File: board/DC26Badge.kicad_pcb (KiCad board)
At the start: 2 copper layers, 94 x 46.5 mm, 23 parts, among them J1 PWR_HDR, J2 PWR_CONN, J3 VOLTMETER, J4 AMMETER, J5 Cortex_SWD, SW1 JOYSTICK, SW2 SW_Push, U1 HT16K33-28, U2 BT832

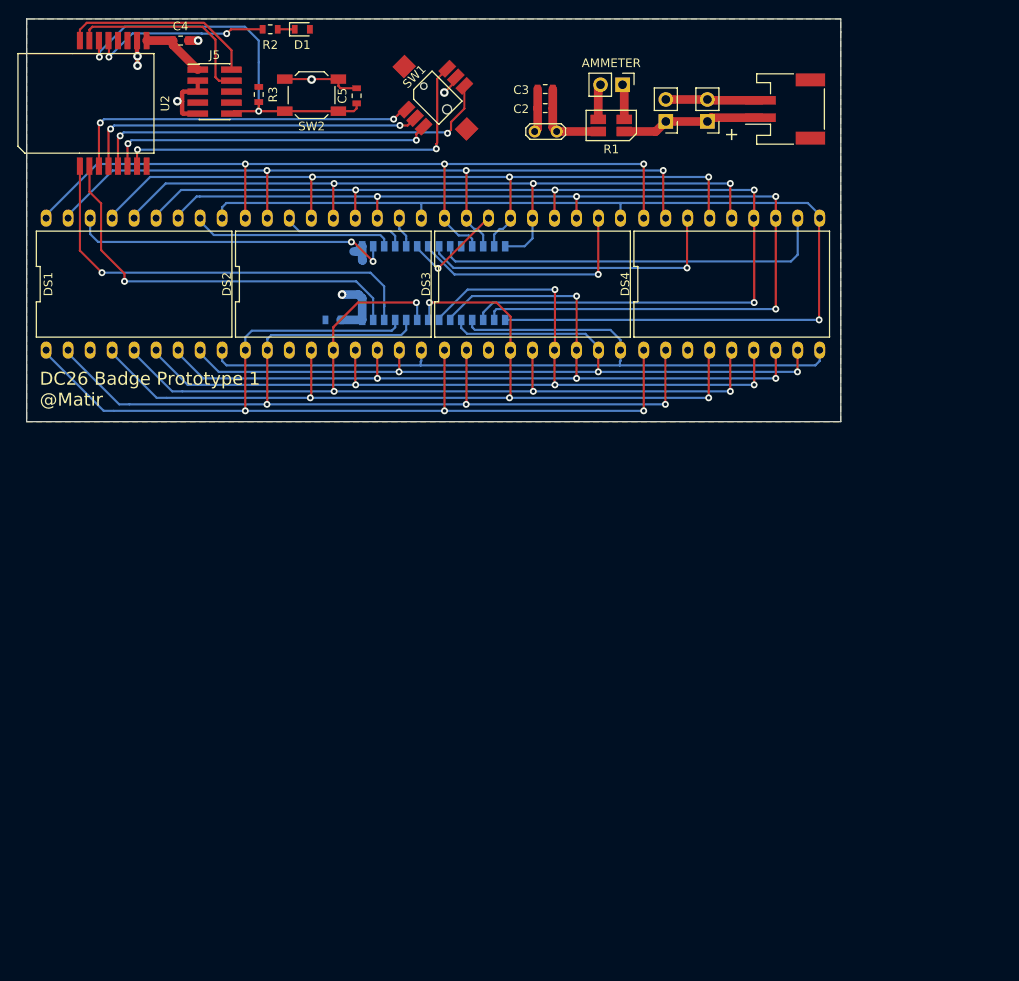
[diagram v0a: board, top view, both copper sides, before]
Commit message: Do first circular board.
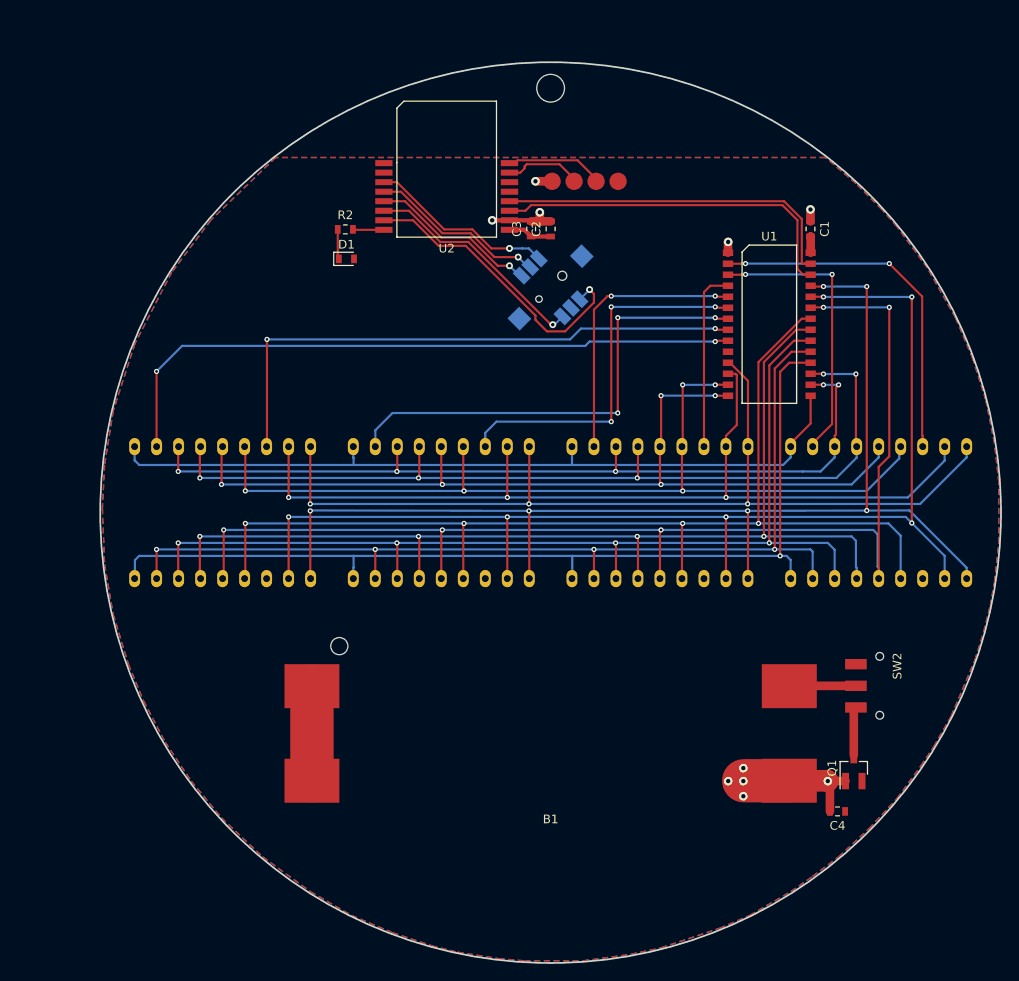
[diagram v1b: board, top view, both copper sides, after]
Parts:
- removed C5: 0.1u, Capacitor_SMD:C_0603_1608Metric
- removed J2: PWR_CONN, Connector_JST:JST_PH_S2B-PH-SM4-TB_1x02_P2.00mm_Horizontal
- removed J3: VOLTMETER, PinHeaders:Pin_Header_Straight_1x02_Pitch2.54mm
- removed J4: AMMETER, PinHeaders:Pin_Header_Straight_1x02_Pitch2.54mm
- removed J5: Cortex_SWD, Connector_PinHeader_1.27mm:PinHeader_2x05_P1.27mm_Vertical_SMD
- removed R1: 0.1, DC26badge:FC4T
- removed R3: 1k, Resistor_SMD:R_0603_1608Metric
- removed TP1: PWRTP, TestPoint:TestPoint_2Pads_Pitch2.54mm_Drill0.8mm
- added B1: Dual_AAA_Holder, DC26badge:Keystone_1022, F.Cu at (155.5, 106.0)
- added G***: LOGO, DC26badge:BG_GLOBE, B.Cu at (155.5, 80.0)
- added MK1: Mounting_Hole, MountingHole:MountingHole_3.2mm_M3, F.Cu at (155.5, 31.5)
- added Q1: SSM3J338, Package_TO_SOT_SMD:SOT-23_Handsoldering, F.Cu at (190.5, 110.0)
- C1: moved to F.Cu
- DS1, DS2, DS3, DS4, SW1: moved to B.Cu
- J1: value PWR_HDR -> SWD_POGO; footprint PinHeaders:Pin_Header_Straight_1x02_Pitch2.54mm -> DC26badge:SWD_POGO
- SW2: value SW_Push -> SW_SPDT; footprint Button_Switch_SMD:SW_SPST_SKQG -> DC26badge:JS102011SAQN
- U1: footprint DC26badge:SOIC-28-300mil -> DC26badge:HT16K133; moved to F.Cu
- moved C4 116.9 mm to (188.6, 115.0), turned to 180 degrees
- moved SW2 94.6 mm to (193.5, 100.5), turned to 90 degrees
- moved DS1 89.9 mm to (193.4, 80.5), turned to 180 degrees
- moved DS4 64.4 mm to (117.6, 80.5), turned to 180 degrees
- moved C1 56.1 mm to (185.5, 47.8), turned to 270 degrees
- moved DS2 46.0 mm to (168.1, 80.5), turned to 180 degrees
- moved U2 40.0 mm to (143.5, 44.0), turned to 270 degrees
- moved U1 39.0 mm to (180.8, 58.8), turned to 270 degrees
- moved DS3 28.4 mm to (142.9, 80.5), turned to 180 degrees
- moved D1 27.0 mm to (131.9, 51.2)
- moved SW1 25.6 mm to (155.5, 54.5), turned to 45 degrees
- moved R2 24.7 mm to (131.8, 47.8), turned to 0 degrees
- moved C3 16.2 mm to (153.2, 47.8), turned to 90 degrees
- moved J1 15.7 mm to (159.5, 42.2)
- moved C2 14.0 mm to (155.5, 47.8), turned to 90 degrees
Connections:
- J1 pad 1: /P_IN -> VDD
- J1 pad 2: GND -> /SWDIO
- SW2 pad 1: /RESET -> Net-(Q1-Pad3)
- SW2 pad 2: GND -> Net-(B1-Pad1)
- U2 pad 1: /SCL -> Net-(U2-Pad1)
- U2 pad 11: Net-(U2-Pad11) -> /SCL
- U2 pad 12: Net-(U2-Pad12) -> /SDA
- U2 pad 13: /LED1 -> Net-(U2-Pad13)
- U2 pad 2: /SDA -> Net-(U2-Pad2)
- U2 pad 3: /UP -> /LT
- U2 pad 5: /DN -> /UP
- U2 pad 6: /LT -> /RT
- U2 pad 7: /RT -> /DN
- U2 pad 8: Net-(U2-Pad8) -> /LED1
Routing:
- net /RESET: track 47.3 -> 0.00 mm, vias 2 -> 0
- net /N: track 100.9 -> 138.8 mm, vias 4 -> 5
- net /B: track 123.0 -> 90.3 mm, vias 1 -> 0
- net /DIG4: track 11.9 -> 43.4 mm, vias 1 -> 3
- net /DIG6: track 35.9 -> 66.2 mm, vias 1 -> 2
- net /DIG7: track 46.1 -> 76.1 mm, vias 0 -> 2
- net /L: track 109.7 -> 139.6 mm, vias 3 -> 6
- net /DIG3: track 3.58 -> 32.0 mm, vias 0 -> 2
- net /DIG5: track 27.6 -> 54.5 mm, vias 1 -> 3
- net /A: track 121.9 -> 96.9 mm, vias 4 -> 5
- net /M: track 104.0 -> 127.1 mm
- net /E: track 113.3 -> 135.7 mm, vias 3 -> 6
- net /UP: track 41.7 -> 19.5 mm, vias 2 -> 1
- net /G1: track 122.8 -> 103.1 mm, vias 4 -> 5
- net /RT: track 46.2 -> 26.6 mm, vias 2 -> 1
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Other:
- board size 94 x 46.5 mm -> 104 x 104 mm
- rule via_min_size: 0.4 -> 0.6
- board text removed: "+"
- board text removed: "DC26 Badge Prototype 1 @Matir"

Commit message: Add copyright.
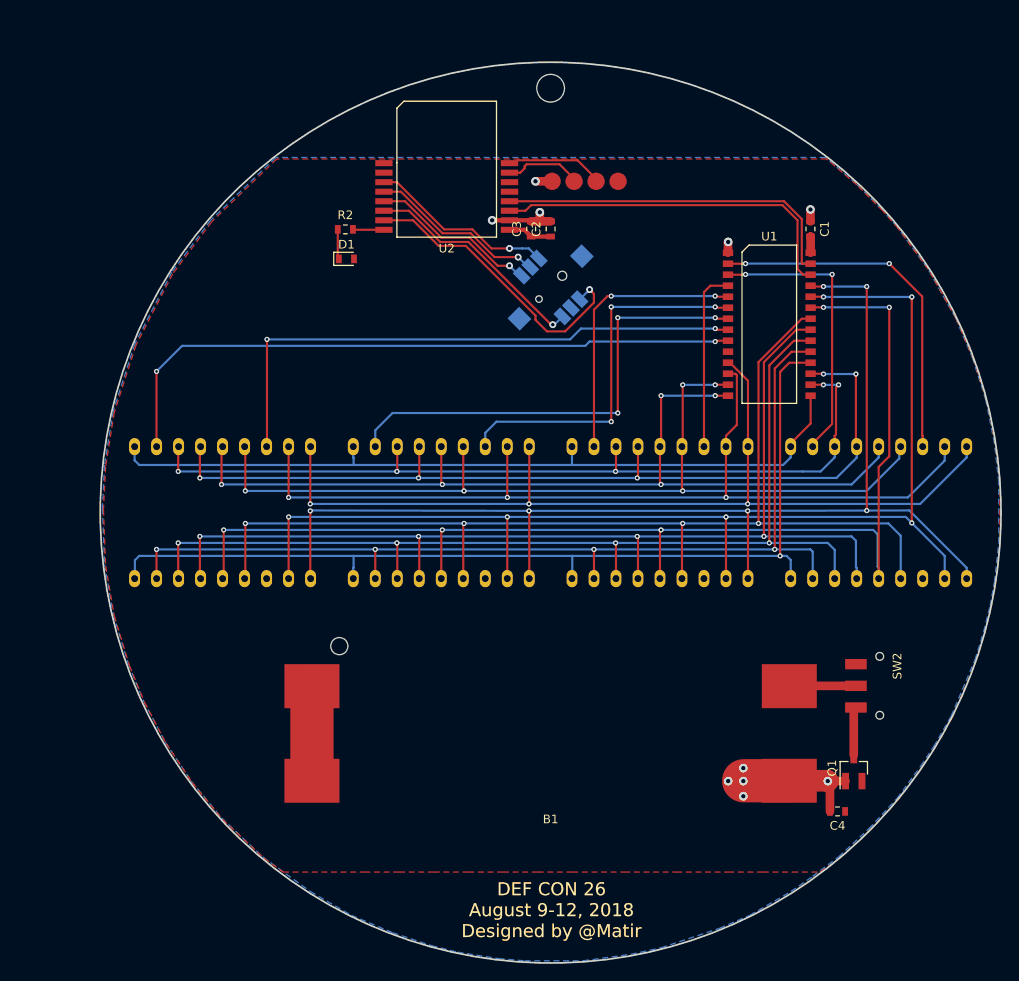
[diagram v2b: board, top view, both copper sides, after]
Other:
- board text added: "DEF CON 26 August 9-12, 2018 Designed by @Matir"
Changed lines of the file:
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@@
   (general
     (thickness 1.6)
-    (drawings 1)
+    (drawings 3)
     (tracks 499)
     (zones 0)
@@
       (xy 2.655607 -45.401114)) (layer B.SilkS) (width 0.01))
   )
+  (gr_text "DEF CON 26\nAugust 9-12, 2018\nDesigned by @Matir" (at 155.6 126.4) (layer F.SilkS)
+    (effects (font (size 1.5 1.5) (thickness 0.3)))
+  )
+  (gr_text "DEF CON 26\nAugust 9-12, 2018\nDesigned by @Matir" (at 155.6 126.4) (layer F.Cu)
+    (effects (font (size 1.5 1.5) (thickness 0.3)))
+  )
   (gr_circle (center 155.5 80.5) (end 207.5 80.5) (layer Edge.Cuts) (width 0.2))
   (segment (start 175.98 49.27) (end 176 49.25) (width 1) (layer F.Cu) (net 1))
@@
     )
   )
-  (zone (net 2) (net_name VDD) (layer F.Cu) (hatch edge 0.508)
-    (connect_pads (clearance 0.254))
-    (min_thickness 0.254)
-    (fill yes (arc_segments 16) (thermal_gap 0.254) (thermal_bridge_width 0.3))
-    (polygon
-      (pts
-        (xy 123.75 39.5) (xy 116.25 46.75) (xy 111.75 52.75) (xy 107.5 61) (xy 105 68.75)
-        (xy 104 75) (xy 103.75 80) (xy 104 86.5) (xy 105 92.25) (xy 106.75 98)
-        (xy 108.5 102.25) (xy 111 107) (xy 114 111.5) (xy 117.5 115.75) (xy 122.25 120.25)
-        (xy 127.75 124.25) (xy 132.5 127) (xy 137.25 129) (xy 141.75 130.5) (xy 144.75 131.25)
-        (xy 149.5 132) (xy 152.5 132.25) (xy 159.25 132.25) (xy 164.75 131.5) (xy 168.25 130.75)
-        (xy 175 128.5) (xy 178.5 127) (xy 183.25 124.25) (xy 185.75 122.5) (xy 188.75 120.25)
-        (xy 192.25 117) (xy 195.5 113.5) (xy 198.25 109.75) (xy 199.75 107.5) (xy 201.75 104)
-        (xy 204.5 97.5) (xy 205.5 94.25) (xy 206.25 91.25) (xy 206.75 88.5) (xy 207.25 84)
-        (xy 207.25 77) (xy 206.75 72.5) (xy 205.75 67.5) (xy 204.25 62.75) (xy 202.25 58)
-        (xy 199 52.25) (xy 195.5 47.5) (xy 193.75 45.5) (xy 190.75 42.5) (xy 187.25 39.5)
-      )
-    )
-  )
   (zone (net 1) (net_name GND) (layer B.Cu) (hatch edge 0.508)
     (connect_pads (clearance 0.254))
@@
       )
     )
+  )
+  (zone (net 2) (net_name VDD) (layer F.Cu) (hatch edge 0.508)
+    (connect_pads (clearance 0.254))
+    (min_thickness 0.254)
+    (fill yes (arc_segments 16) (thermal_gap 0.254) (thermal_bridge_width 0.3))
+    (polygon
+      (pts
+        (xy 123.870179 39.671493) (xy 116.370179 46.921493) (xy 111.870179 52.921493) (xy 107.620179 61.171493) (xy 105.120179 68.921493)
+        (xy 104.120179 75.171493) (xy 103.870179 80.171493) (xy 104.120179 86.671493) (xy 105.120179 92.421493) (xy 106.870179 98.171493)
+        (xy 108.620179 102.421493) (xy 111.120179 107.171493) (xy 114.120179 111.671493) (xy 117.620179 115.921493) (xy 122.4 120.4)
+        (xy 124.6 122) (xy 134 122) (xy 138 122) (xy 142 122) (xy 146 122)
+        (xy 150 122) (xy 154 122) (xy 158 122) (xy 164 122) (xy 170 122)
+        (xy 176 122) (xy 180 122) (xy 183.4 122) (xy 186.6 122) (xy 188.870179 120.421493)
+        (xy 192.370179 117.171493) (xy 195.620179 113.671493) (xy 198.370179 109.921493) (xy 199.870179 107.671493) (xy 201.870179 104.171493)
+        (xy 204.620179 97.671493) (xy 205.620179 94.421493) (xy 206.370179 91.421493) (xy 206.870179 88.671493) (xy 207.370179 84.171493)
+        (xy 207.370179 77.171493) (xy 206.870179 72.671493) (xy 205.870179 67.671493) (xy 204.370179 62.921493) (xy 202.370179 58.171493)
+        (xy 199.120179 52.421493) (xy 195.620179 47.671493) (xy 193.870179 45.671493) (xy 190.870179 42.671493) (xy 187.370179 39.671493)
+      )
+    )

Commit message: Fix silkscreen.
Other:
- board text added: "GND SWDCLK SWDIO VCC"
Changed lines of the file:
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@@
   (general
     (thickness 1.6)
-    (drawings 3)
+    (drawings 4)
     (tracks 499)
     (zones 0)
@@
     (tags capacitor)
     (attr smd)
-    (fp_text reference C1 (at 0 -1.65 270) (layer F.SilkS)
+    (fp_text reference C1 (at 0 -1.65) (layer F.SilkS)
       (effects (font (size 1 1) (thickness 0.15)))
     )
@@
     (tags capacitor)
     (attr smd)
-    (fp_text reference C2 (at 0 -1.65 90) (layer F.SilkS)
+    (fp_text reference C2 (at -0.65 2.9 180) (layer F.SilkS)
       (effects (font (size 1 1) (thickness 0.15)))
     )
@@
     (tags capacitor)
     (attr smd)
-    (fp_text reference C3 (at 0 -1.65 90) (layer F.SilkS)
+    (fp_text reference C3 (at 0.75 5.15 180) (layer F.SilkS)
       (effects (font (size 1 1) (thickness 0.15)))
     )
@@
     (tags SOT-23)
     (attr smd)
-    (fp_text reference Q1 (at 0 -2.5 90) (layer F.SilkS)
+    (fp_text reference Q1 (at 1.6 -2.3 180) (layer F.SilkS)
       (effects (font (size 1 1) (thickness 0.15)))
     )
@@
   (module DC26badge:JS102011SAQN (layer F.Cu)
     (at 193.5 100.5 90)
-    (fp_text reference SW2 (at 2.286 2.032 90) (layer F.SilkS)
+    (fp_text reference SW2 (at -0.1 0.3 180) (layer F.SilkS)
       (effects (font (size 1 1) (thickness 0.15)))
     )
@@
       (xy 2.655607 -45.401114)) (layer B.SilkS) (width 0.01))
   )
+  (gr_text "GND\n\nSWDCLK\n\nSWDIO\n\nVCC" (at 159.6 40.6 90) (layer F.SilkS)
+    (effects (font (size 0.8 0.8) (thickness 0.12)) (justify left))
+  )
   (gr_text "DEF CON 26\nAugust 9-12, 2018\nDesigned by @Matir" (at 155.6 126.4) (layer F.SilkS)

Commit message: Fix up board.
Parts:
- added J2: SWD, Connector_PinHeader_1.27mm:PinHeader_2x05_P1.27mm_Vertical_SMD, F.Cu at (139.4, 56.0)
- added REF**: OSHW-Logo_7.5x8mm_SilkScreen, Symbol:OSHW-Logo_7.5x8mm_SilkScreen, F.Cu at (116.4, 98.3)
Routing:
- net GND: track 27.8 -> 50.6 mm, vias 10 -> 13
- net /SWDCLK: track 8.76 -> 29.7 mm
- net /SWDIO: track 11.1 -> 30.9 mm
- net /DN: track 34.6 -> 32.3 mm
- added copper zone on F.Cu, net GND
